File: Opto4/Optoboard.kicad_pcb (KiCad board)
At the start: 2 copper layers, 68 x 35 mm, 41 parts, among them J1 S1 Connector, J2 S2 Connector, J3 S3 Connector, J4 S4 Connector, J5 Conn_01x06, Q1 IRLR024NPBF, U1 6N135, U2 6N135, U3 6N135, U4 6N135

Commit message: Added fancy
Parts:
- renumbered U1 to U1-6N135, U2 to U2-6N135, U3 to U3-6N135, U4 to U4-6N135
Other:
- board text added: "Elektropioneer github.com/Elektropioneer"
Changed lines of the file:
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@@
     (area 158.924999 90.924999 227.075001 126.075001)
     (thickness 1.6)
-    (drawings 29)
+    (drawings 30)
     (tracks 151)
     (zones 0)
@@
   )
   (setup
-    (last_trace_width 0.5)
+    (last_trace_width 0.25)
     (user_trace_width 0.25)
     (user_trace_width 0.5)
@@
     (descr "8-lead though-hole mounted DIP package, row spacing 7.62 mm (300 mils)")
     (tags "THT DIP DIL PDIP 2.54mm 7.62mm 300mil")
-    (fp_text reference U1 (at 3.75 4 180) (layer F.SilkS)
+    (fp_text reference U1-6N135 (at 3.75 4.25 180) (layer F.SilkS)
       (effects (font (size 1 1) (thickness 0.15)))
     )
@@
     (descr "8-lead though-hole mounted DIP package, row spacing 7.62 mm (300 mils)")
     (tags "THT DIP DIL PDIP 2.54mm 7.62mm 300mil")
-    (fp_text reference U2 (at 3.75 3.5 180) (layer F.SilkS)
+    (fp_text reference U2-6N135 (at 3.75 4.25 180) (layer F.SilkS)
       (effects (font (size 1 1) (thickness 0.15)))
     )
@@
     (descr "8-lead though-hole mounted DIP package, row spacing 7.62 mm (300 mils)")
     (tags "THT DIP DIL PDIP 2.54mm 7.62mm 300mil")
-    (fp_text reference U3 (at 3.75 3.5 180) (layer F.SilkS)
+    (fp_text reference U3-6N135 (at 3.75 4 180) (layer F.SilkS)
       (effects (font (size 1 1) (thickness 0.15)))
     )
@@
     (descr "8-lead though-hole mounted DIP package, row spacing 7.62 mm (300 mils)")
     (tags "THT DIP DIL PDIP 2.54mm 7.62mm 300mil")
-    (fp_text reference U4 (at 3.75 3.5 180) (layer F.SilkS)
+    (fp_text reference U4-6N135 (at 3.75 4 180) (layer F.SilkS)
       (effects (font (size 1 1) (thickness 0.15)))
     )
@@
     (fp_circle (center 0 0) (end 0 -2.286) (layer F.SilkS) (width 0.12))
     (pad 1 thru_hole circle (at 0 0) (size 4.064 4.064) (drill 3.048) (layers *.Cu *.Mask))
+  )
+  (gr_text "Elektropioneer\ngithub.com/Elektropioneer" (at 182.5 95.25) (layer F.SilkS)
+    (effects (font (size 0.5 0.5) (thickness 0.125)) (justify left))
   )
   (gr_line (start 227 91) (end 227 91.5) (angle 90) (layer Edge.Cuts) (width 0.15))
@@
   (segment (start 217.2 114.95) (end 217.2 118.53) (width 0.5) (layer F.Cu) (net 4))
   (segment (start 217.2 118.53) (end 218.67 120) (width 0.5) (layer F.Cu) (net 4))
-  (segment (start 209.4 94.6) (end 209.4 93.4) (width 0.5) (layer F.Cu) (net 5) (status 400000))
+  (segment (start 209.4 94.6) (end 209.4 93.4) (width 0.5) (layer F.Cu) (net 5))
   (segment (start 208 92) (end 180.5 92) (width 0.5) (layer F.Cu) (net 5))
   (segment (start 209.4 93.4) (end 208 92) (width 0.5) (layer F.Cu) (net 5))

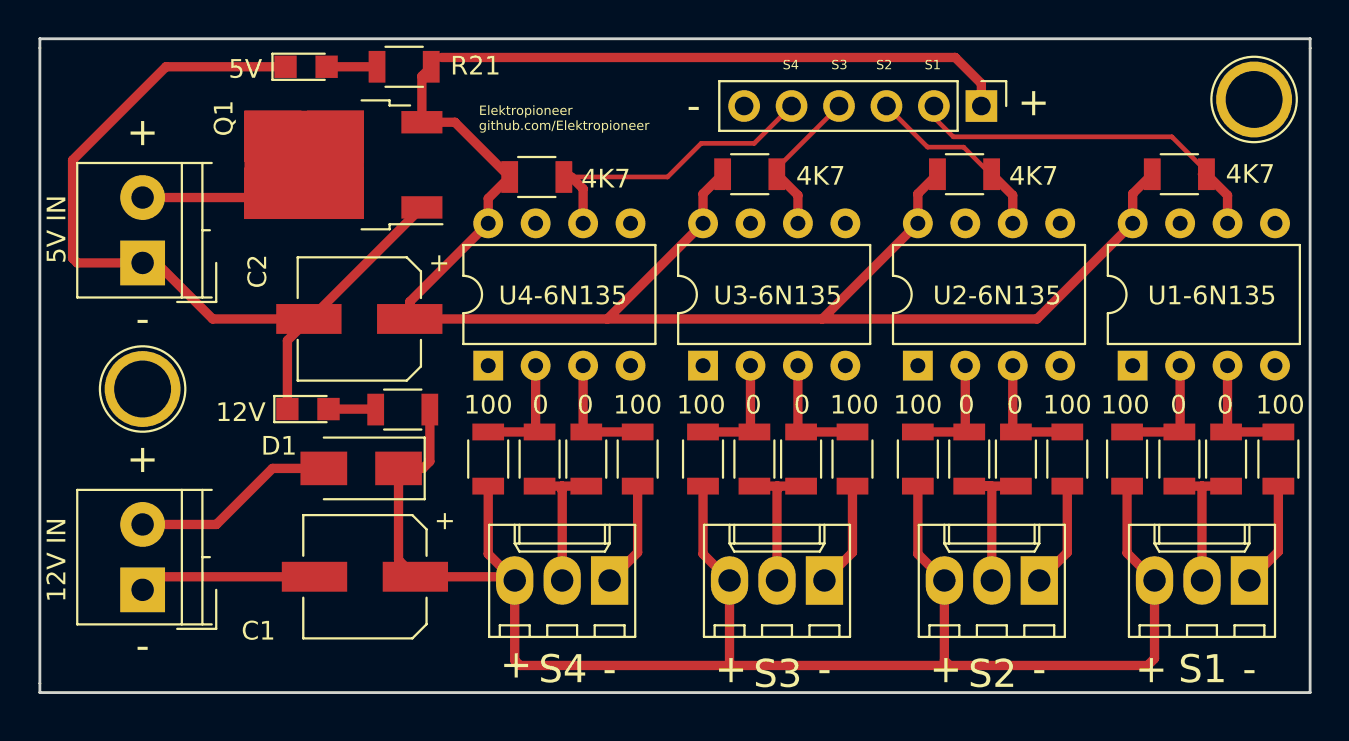
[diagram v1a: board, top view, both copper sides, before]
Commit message: Changed some labels and text
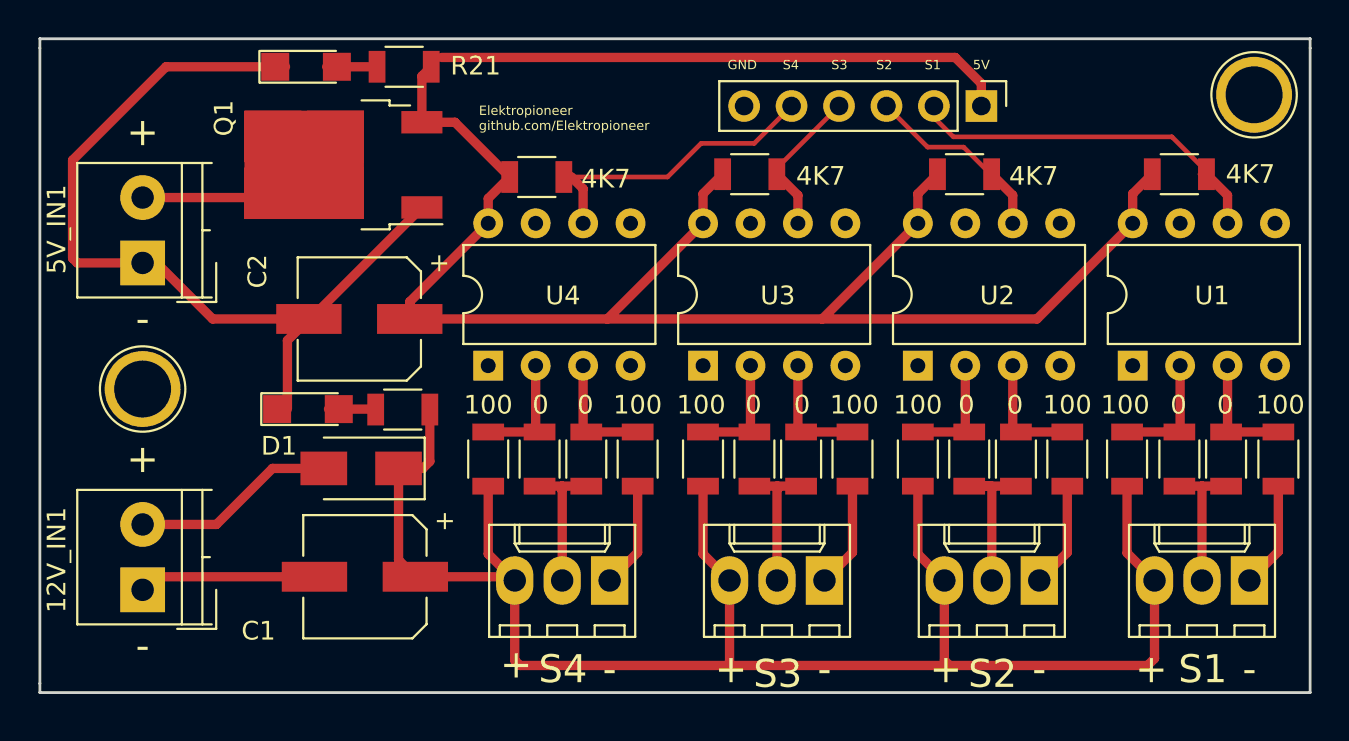
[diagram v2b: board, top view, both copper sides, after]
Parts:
- removed 12V, 5V: LED, LEDs:LED_0805
- added D2: LED, LEDs:LED_1206, F.Cu at (173.2, 92.5)
- added D3: LED, LEDs:LED_1206, F.Cu at (173.3, 110.8)
- 12V_IN1: renamed from 12V IN
- 5V_IN1: renamed from 5V IN
- moved REF** 0.25 mm to (224.0, 94.0)
- renumbered U1-6N135 to U1, U2-6N135 to U2, U3-6N135 to U3, U4-6N135 to U4
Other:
- board text added: "5V"
- board text added: "GND"

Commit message: Changed things that were discussed, also added photos
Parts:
- removed D3: LED, LEDs:LED_1206
- removed R22: R, Resistors_SMD:R_1206
- removed the REF** at (164.5, 109.8)
- removed the REF** at (224.0, 94.0)
- added REF**: 1pin, Connectors:1pin, F.Cu at (164.5, 109.9)
- added REF**: 1pin, Connectors:1pin, F.Cu at (223.5, 94.6)
- 12V IN: renamed from 12V_IN1
- 5V IN: renamed from 5V_IN1
- D1: value D -> STTH2R06U
- D2: value LED -> LED_RED
- moved Q1 1.31 mm to (175.3, 99.1), turned to 0 degrees
- moved D1 1.10 mm to (176.1, 112.9)
- renumbered 0 to R1, 4K7 to R10, 0 to R11, 0 to R12, 0 to R13, 0 to R14, 100 to R15, 100 to R16, 100 to R17, 100 to R18, 4K7 to R19, 0 to R2, 4K7 to R20, 0 to R3, 0 to R4, 100 to R5, 100 to R6, 100 to R7, 100 to R8, 4K7 to R9
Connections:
- 5V IN pad 1: GND -> Net-(5V_IN1-Pad1)
- 5V IN pad 2: Net-(5V_IN1-Pad2) -> +5V
- Q1 pad 1: GND -> +5V
- Q1 pad 2: Net-(5V_IN1-Pad2) -> GND
- Q1 pad 3: +5V -> Net-(5V_IN1-Pad1)
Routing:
- net +5V: track 114.1 -> 132.4 mm
- net GND: track 78.7 -> 68.3 mm, vias 0 -> 2
- net Net-(5V_IN1-Pad2): track 9.37 -> 0.00 mm
- net Net-(5V_IN1-Pad1): track 0.00 -> 8.00 mm
- net +12V: track 91.0 -> 88.1 mm
- net Net-(D3-Pad2): track 2.54 -> 0.00 mm
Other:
- board text added: "D2"
- board text added: "Opto-isolator board Rev: 1.0 - Opto version: 4"
- board text added: "http://elektropioneer.co.rs/ https://github.com/Elektropioneer"
- board text removed: "Elektropioneer github.com/Elektropioneer"

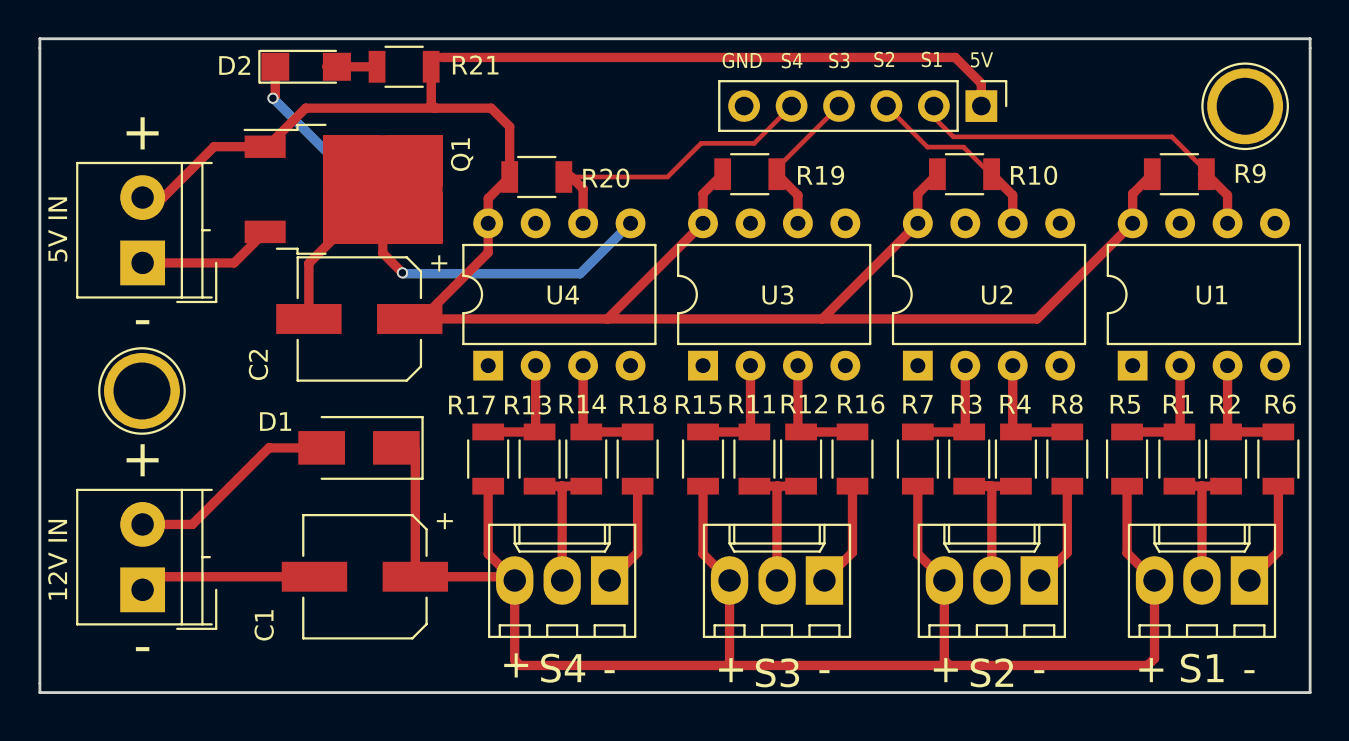
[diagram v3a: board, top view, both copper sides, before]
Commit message: Added mounting hole and some writing, 99% ready
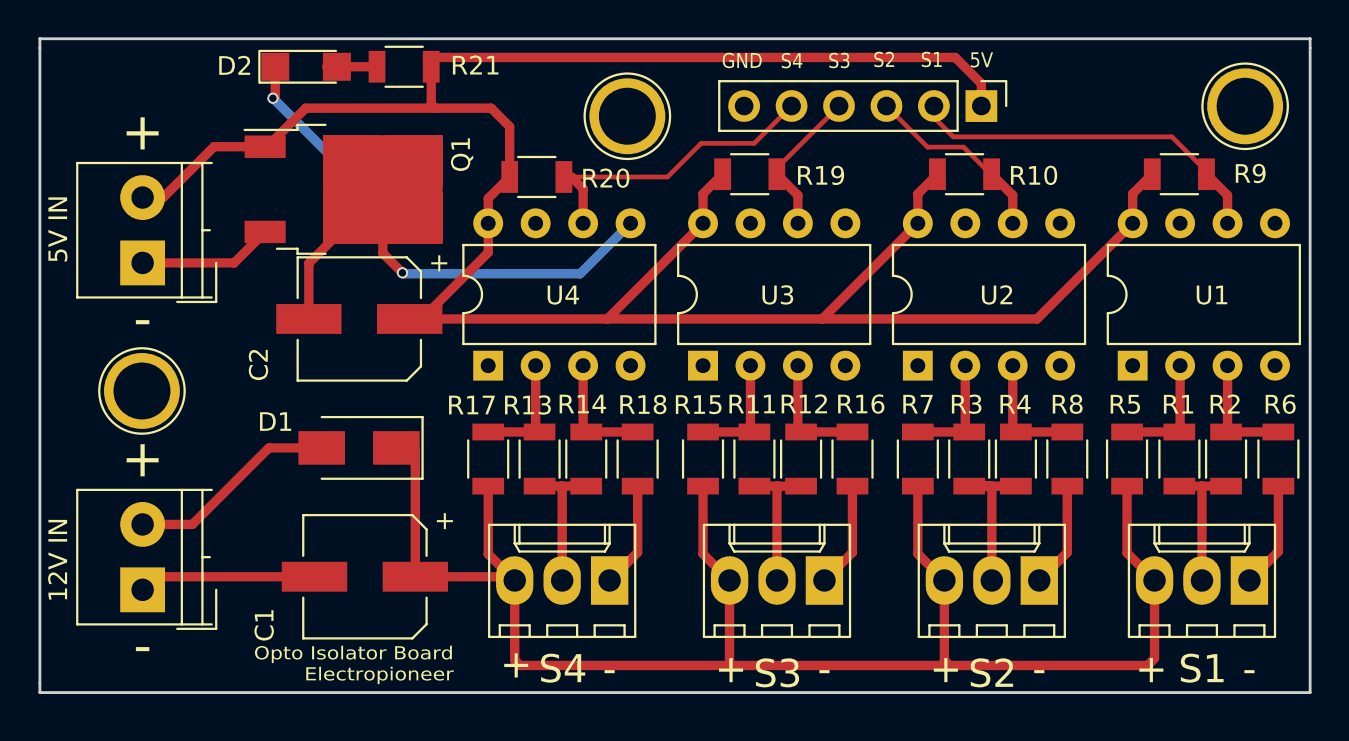
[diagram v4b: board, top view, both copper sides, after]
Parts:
- added REF**: 1pin, Connectors:1pin, F.Cu at (190.4, 95.1)
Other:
- board text added: "Opto Isolator Board Electropioneer"
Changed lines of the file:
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@@
     (area 158.924999 90.924999 227.075001 126.075001)
     (thickness 1.6)
-    (drawings 34)
+    (drawings 35)
     (tracks 158)
     (zones 0)
-    (modules 39)
+    (modules 40)
     (nets 23)
   )
@@
   )
   (setup
-    (last_trace_width 0.5)
+    (last_trace_width 0.25)
     (user_trace_width 0.25)
     (user_trace_width 0.5)
@@
     (mod_text_size 1 1)
     (mod_text_width 0.15)
-    (pad_size 1.524 1.524)
-    (pad_drill 0.762)
+    (pad_size 2.4 2.4)
+    (pad_drill 1.2)
     (pad_to_mask_clearance 0.2)
     (aux_axis_origin 0 0)
+    (grid_origin 196.1388 103.4796)
     (visible_elements FFFFFF7F)
     (pcbplotparams
@@
     (fp_circle (center 0 0) (end 0 -2.286) (layer F.SilkS) (width 0.12))
     (pad 1 thru_hole circle (at 0 0) (size 4.064 4.064) (drill 3.048) (layers *.Cu *.Mask))
+  )
+  (module Connectors:1pin (layer F.Cu)
+    (at 190.4492 95.1484)
+    (descr "module 1 pin (ou trou mecanique de percage)")
+    (tags DEV)
+    (fp_text reference REF** (at 0 -3.048) (layer F.SilkS) hide
+      (effects (font (size 1 1) (thickness 0.15)))
+    )
+    (fp_text value 1pin (at 0 3) (layer F.Fab) hide
+      (effects (font (size 1 1) (thickness 0.15)))
+    )
+    (fp_circle (center 0 0) (end 2 0.8) (layer F.Fab) (width 0.1))
+    (fp_circle (center 0 0) (end 2.6 0) (layer F.CrtYd) (width 0.05))
+    (fp_circle (center 0 0) (end 0 -2.286) (layer F.SilkS) (width 0.12))
+    (pad 1 thru_hole circle (at 0 0) (size 4.064 4.064) (drill 3.048) (layers *.Cu *.Mask))
+  )
+  (gr_text "Opto Isolator Board\nElectropioneer" (at 181.1528 124.46) (layer F.SilkS)
+    (effects (font (size 0.7 0.8) (thickness 0.175)) (justify right))
   )
   (gr_text "D2\n" (at 169.4307 92.4687) (layer F.SilkS)
@@
   (segment (start 164.5 103) (end 165.25 103) (width 0.5) (layer F.Cu) (net 22))
   (zone (net 1) (net_name GND) (layer B.Cu) (hatch edge 0.508)
-    (connect_pads (clearance 0.508))
+    (connect_pads yes (clearance 0.508))
     (min_thickness 0.254)
     (fill yes (arc_segments 16) (thermal_gap 0.508) (thermal_bridge_width 0.508))
     (polygon
       (pts
-        (xy 227 91) (xy 227 126) (xy 159 126) (xy 159 91)
+        (xy 227 126) (xy 159 126) (xy 159 91) (xy 227 91) (xy 227 126)
       )
     )
